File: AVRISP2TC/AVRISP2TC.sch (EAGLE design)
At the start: 13 parts, among them U1 NCP1117LPST33T3G

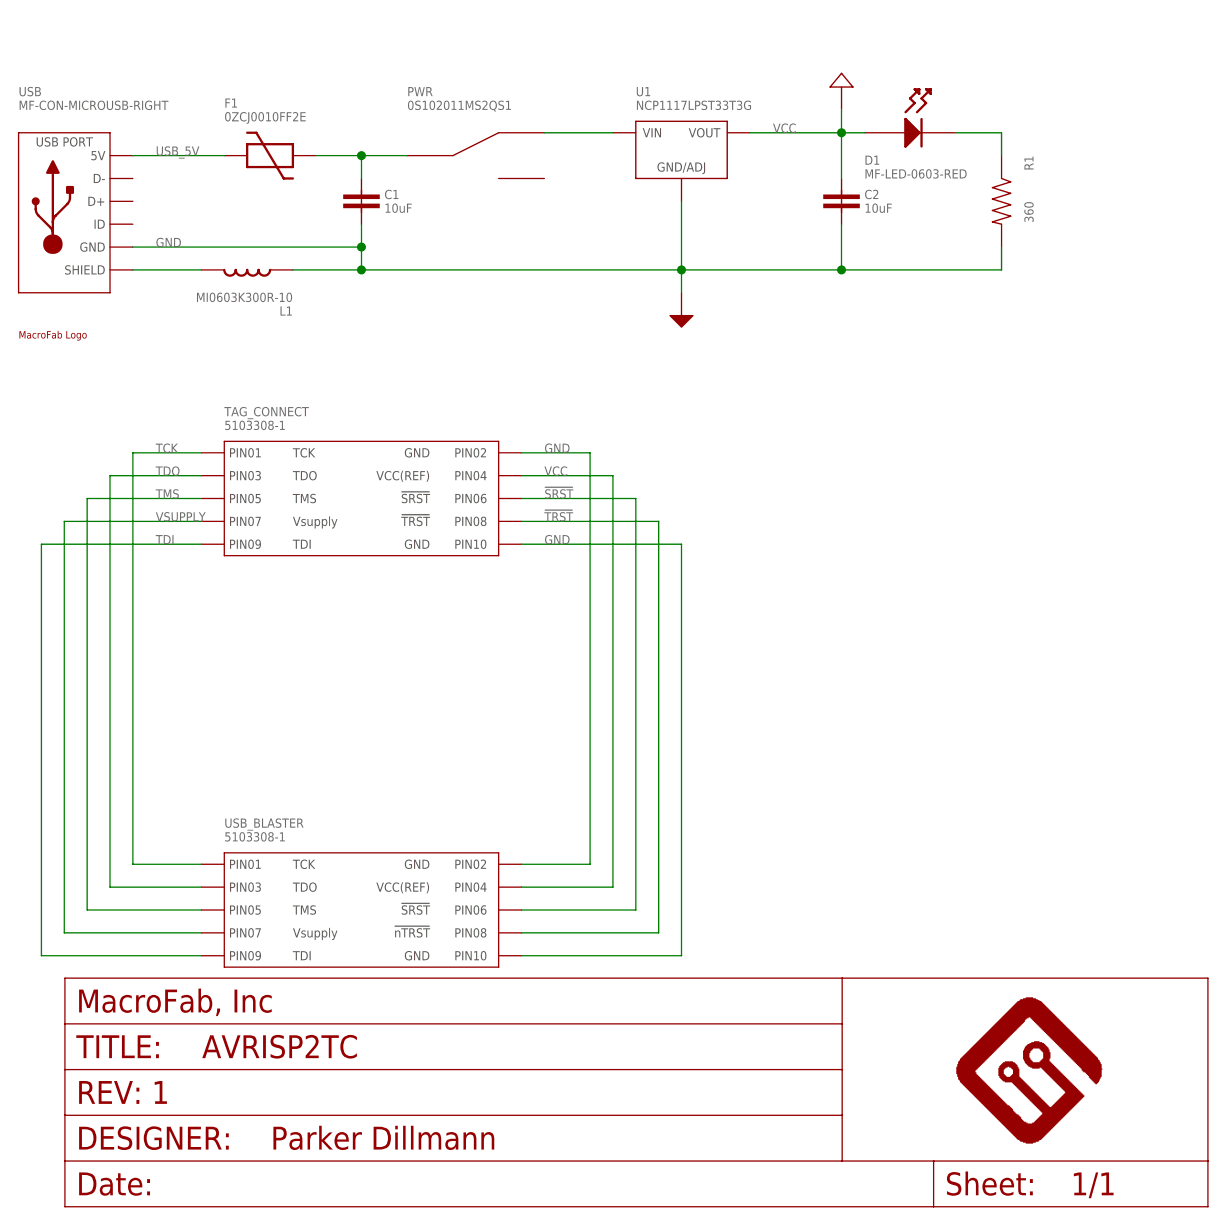
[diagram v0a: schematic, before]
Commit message: Added AVRISP2TC
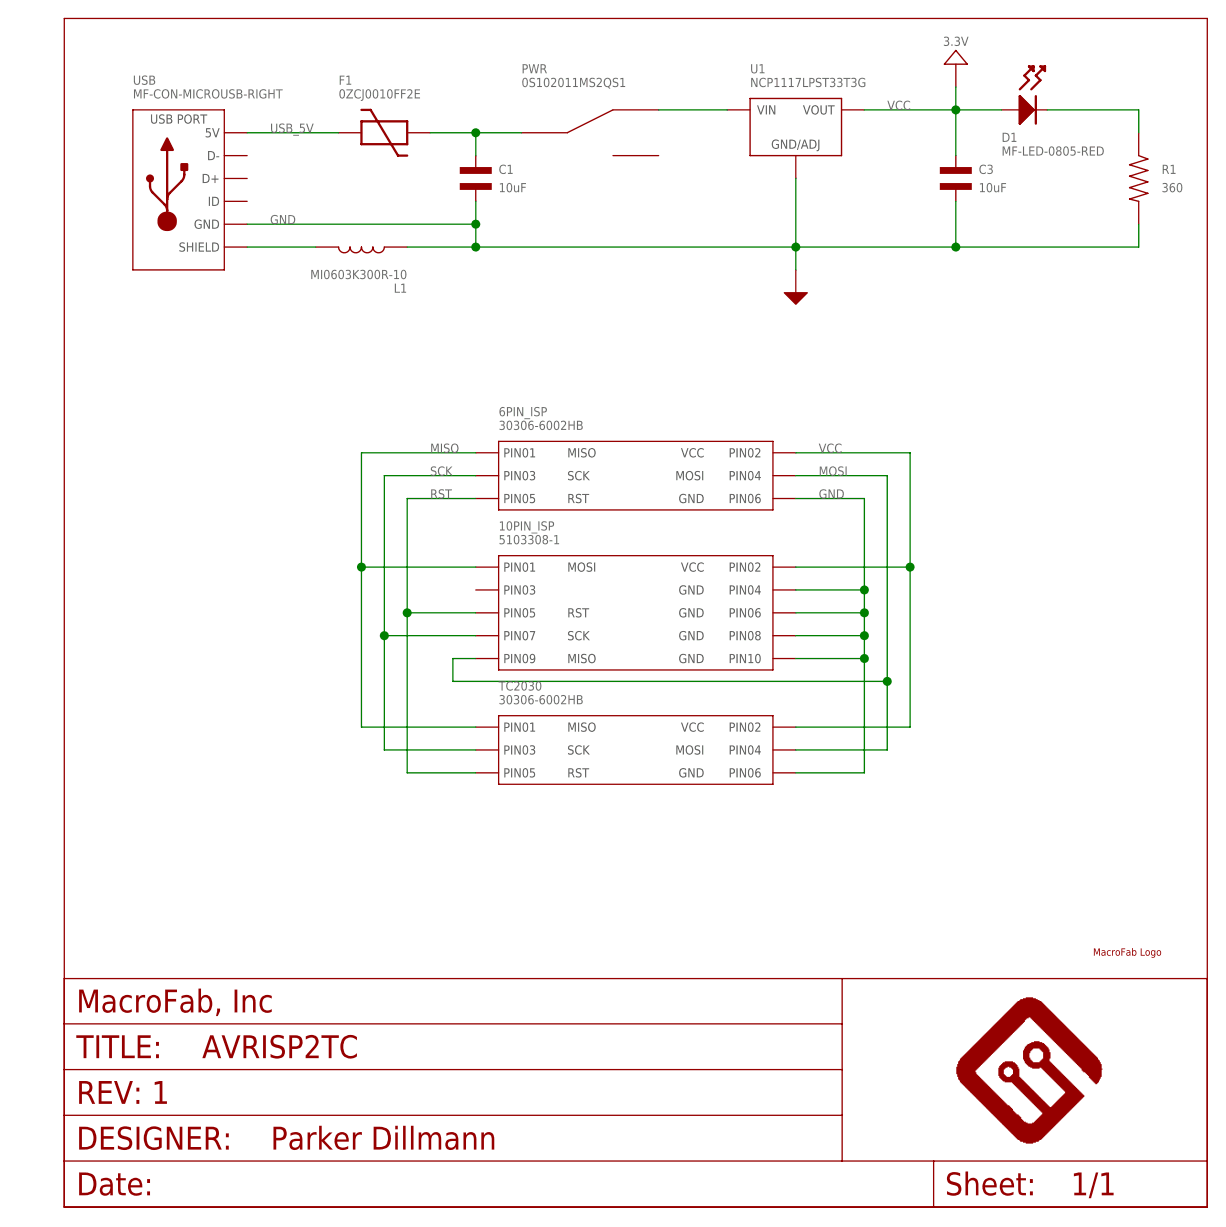
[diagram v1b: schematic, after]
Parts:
- removed C2: 10uF, PP_Passives:CAPACITOR_NON_POLAR_1206
- removed TAG_CONNECT, USB_BLASTER: 5103308-1, PP_Connectors:CON_02X05_5103308-1
- added 10PIN_ISP: 5103308-1, PP_Connectors:CON_02X05_5103308-1
- added 6PIN_ISP, TC2030: 30306-6002HB, PP_Connectors:CON_02X03_30306-6002HB
- added C3: 10uF, MF_Passives:CAPACITOR_NP_1206
- C1: device PP_Passives:CAPACITOR_NON_POLAR_1206 -> MF_Passives:CAPACITOR_NP_1206; MPN (none) -> MF-CAP-1206-10uF
- D1: value MF-LED-0603-RED -> MF-LED-0805-RED; device MF_LEDs:LED_SINGLE_0805 -> MF_LEDs:LED_SINGLE-0805-RED
- F1: MPN (none) -> 0ZCJ0010FF2E; POPULATE (none) -> 1
- L1: MPN (none) -> MI0603K300R-10
- PWR: MPN (none) -> 0S102011MS2QS1; POPULATE (none) -> 1
- R1: MPN (none) -> MF-RES-0805-360
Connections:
- removed net !SRST: TAG_CONNECT.PIN6, USB_BLASTER.PIN6
- removed net !TRST: TAG_CONNECT.PIN8, USB_BLASTER.PIN8
- removed net TCK: TAG_CONNECT.PIN1, USB_BLASTER.PIN1
- removed net TDI: TAG_CONNECT.PIN9, USB_BLASTER.PIN9
- removed net TDO: TAG_CONNECT.PIN3, USB_BLASTER.PIN3
- removed net TMS: TAG_CONNECT.PIN5, USB_BLASTER.PIN5
- removed net VSUPPLY: TAG_CONNECT.PIN7, USB_BLASTER.PIN7
- new net MISO: 10PIN_ISP.PIN1, 6PIN_ISP.PIN1, TC2030.PIN1
- new net MOSI: 10PIN_ISP.PIN9, 6PIN_ISP.PIN4, TC2030.PIN4
- new net RST: 10PIN_ISP.PIN5, 6PIN_ISP.PIN5, TC2030.PIN5
- new net SCK: 10PIN_ISP.PIN7, 6PIN_ISP.PIN3, TC2030.PIN3
- net GND: now also 10PIN_ISP.PIN10, 10PIN_ISP.PIN4, 10PIN_ISP.PIN6, 10PIN_ISP.PIN8, 6PIN_ISP.PIN6, C1.P$2, C3.P$2, TC2030.PIN6; no longer C1.2, C2.2, TAG_CONNECT.PIN10, TAG_CONNECT.PIN2, USB_BLASTER.PIN10, USB_BLASTER.PIN2
- net N$2: now also C1.P$1; no longer C1.1
- net VCC: now also 10PIN_ISP.PIN2, 6PIN_ISP.PIN2, C3.P$1, TC2030.PIN2; no longer C2.1, TAG_CONNECT.PIN4, USB_BLASTER.PIN4
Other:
- moved on the sheet: D1, F1, L1, PWR, R1, U1, USB
